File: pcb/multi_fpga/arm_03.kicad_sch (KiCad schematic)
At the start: 16 parts, among them U25 IM72D128V01XTMA1, U26 IM72D128V01XTMA1, U27 IM72D128V01XTMA1, U28 IM72D128V01XTMA1, U29 IM72D128V01XTMA1, U30 IM72D128V01XTMA1, U31 IM72D128V01XTMA1, U32 IM72D128V01XTMA1

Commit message: Fixed library and power issues.
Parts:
- C25, C26, C27, C28, C29, C30, C31, C32: symbol C -> multi_fpga:C
- U25, U26, U27, U28, U29, U30, U31, U32: symbol IM72D128 -> multi_fpga:IM72D128

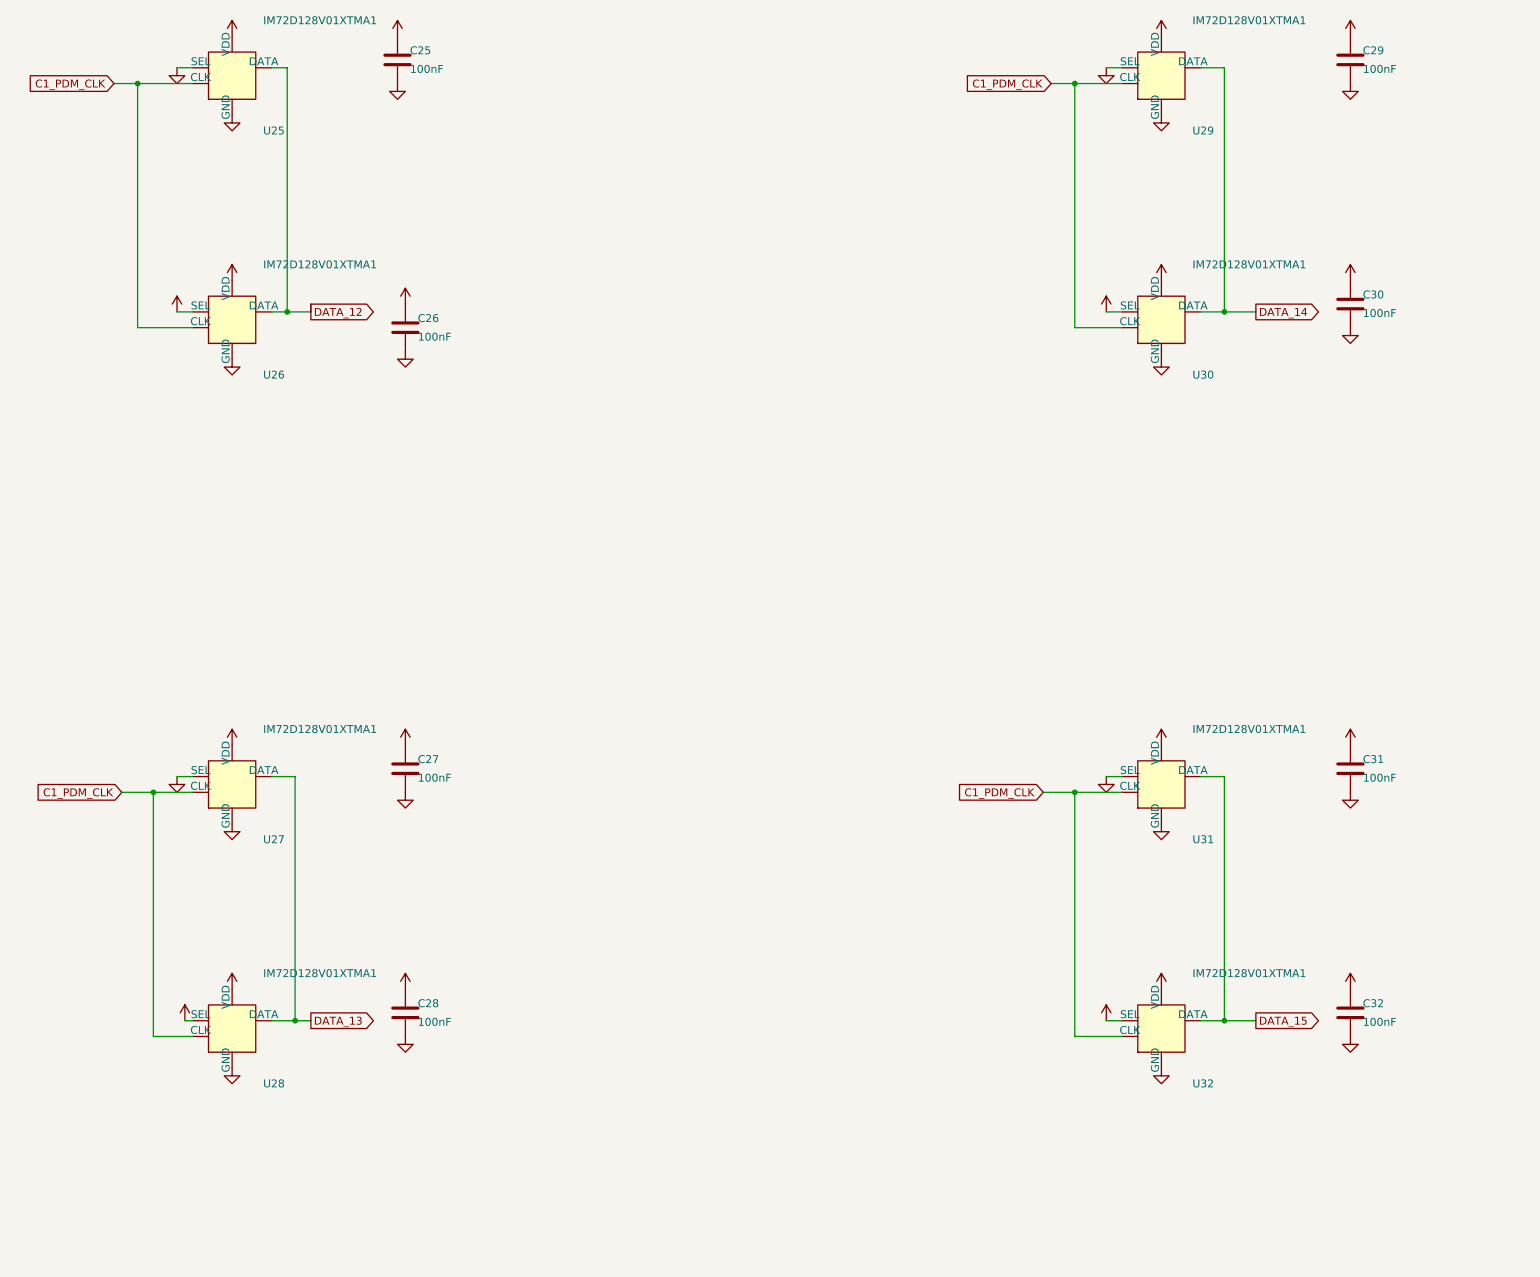
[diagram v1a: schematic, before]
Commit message: Fixed power and C ref des collisions.
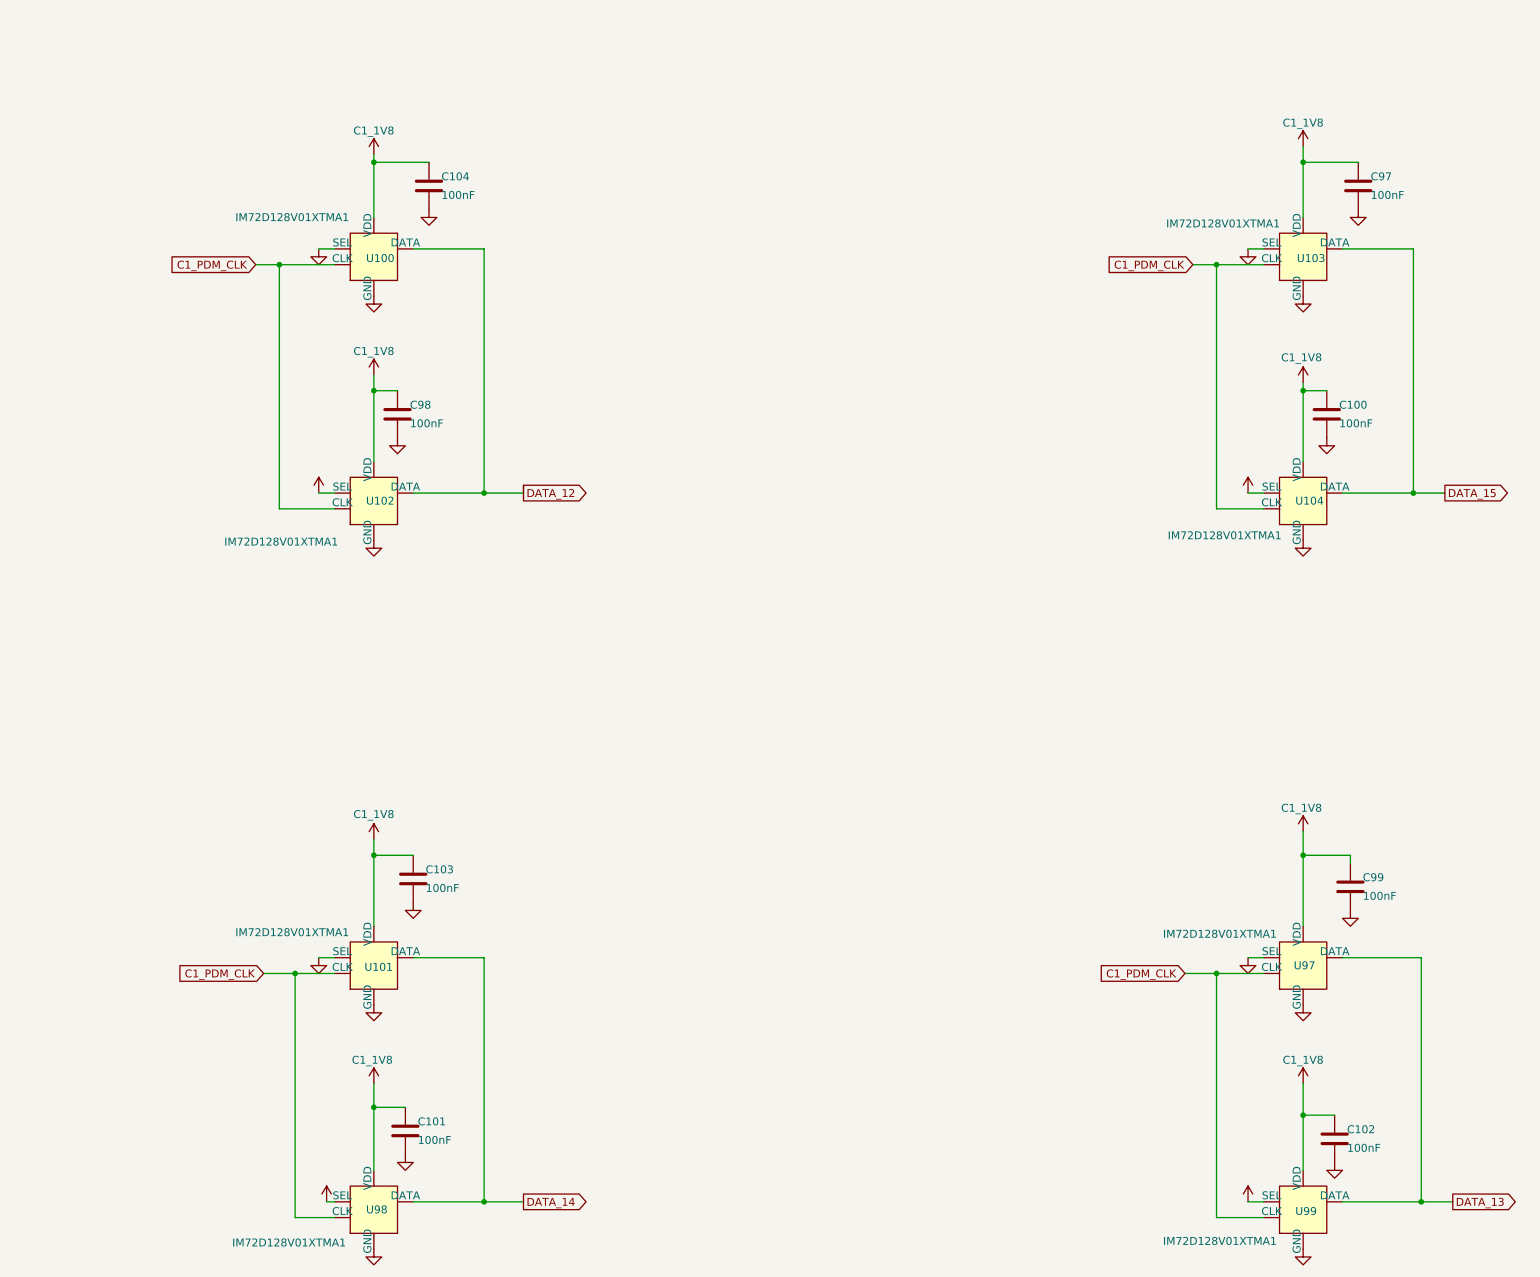
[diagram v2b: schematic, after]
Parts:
- removed C25, C26, C27, C28, C29, C30, C31, C32: 100nF, symbol multi_fpga:C
- removed U25, U26, U27, U28, U29, U30, U31, U32: IM72D128V01XTMA1, symbol multi_fpga:IM72D128
- added C100, C101, C102, C103, C104, C97, C98, C99: 100nF, symbol multi_fpga:C
- added U100, U101, U102, U103, U104, U97, U98, U99: IM72D128V01XTMA1, symbol multi_fpga:IM72D128
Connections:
- net C1_1V8: now also C100.1, C101.1, C102.1, C103.1, C104.1, C97.1, C98.1, C99.1, U100.2 (VDD), U101.2 (VDD), U102.2 (VDD), U102.4 (SEL), U103.2 (VDD), U104.2 (VDD), U104.4 (SEL), U97.2 (VDD), U98.2 (VDD), U98.4 (SEL), U99.2 (VDD), U99.4 (SEL)
- net C1_PDM_CLK: now also U100.3 (CLK), U101.3 (CLK), U102.3 (CLK), U103.3 (CLK), U104.3 (CLK), U97.3 (CLK), U98.3 (CLK), U99.3 (CLK)
- net DATA_12: now also U100.1 (DATA), U102.1 (DATA)
- net DATA_13: now also U97.1 (DATA), U99.1 (DATA)
- net DATA_14: now also U101.1 (DATA), U98.1 (DATA)
- net DATA_15: now also U103.1 (DATA), U104.1 (DATA)
- net GND: now also C100.2, C101.2, C102.2, C103.2, C104.2, C97.2, C98.2, C99.2, U100.4 (SEL), U100.5 (GND), U101.4 (SEL), U101.5 (GND), U102.5 (GND), U103.4 (SEL), U103.5 (GND), U104.5 (GND), U97.4 (SEL), U97.5 (GND), U98.5 (GND), U99.5 (GND)

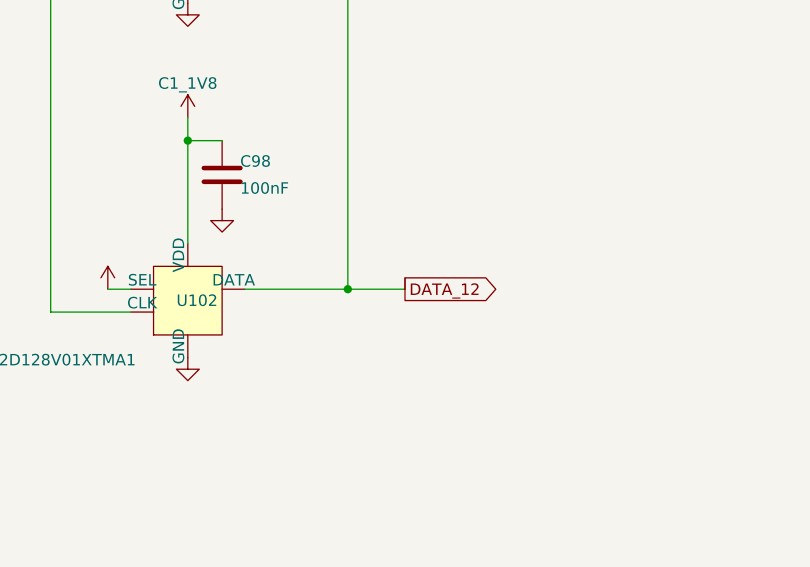
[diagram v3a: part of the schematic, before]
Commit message: Fixed regulator connection errors and dangling wire.
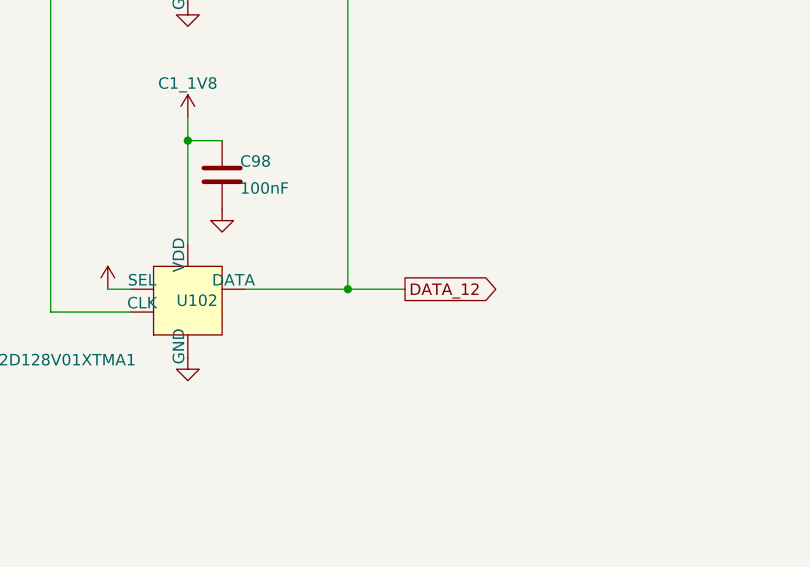
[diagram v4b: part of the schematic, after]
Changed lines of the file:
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@@
-	(wire
-		(pts
-			(xy 127 106.68) (xy 127 107.95)
-		)
-		(stroke
-			(width 0)
-			(type default)
-		)
-	)
 	(wire
 		(pts

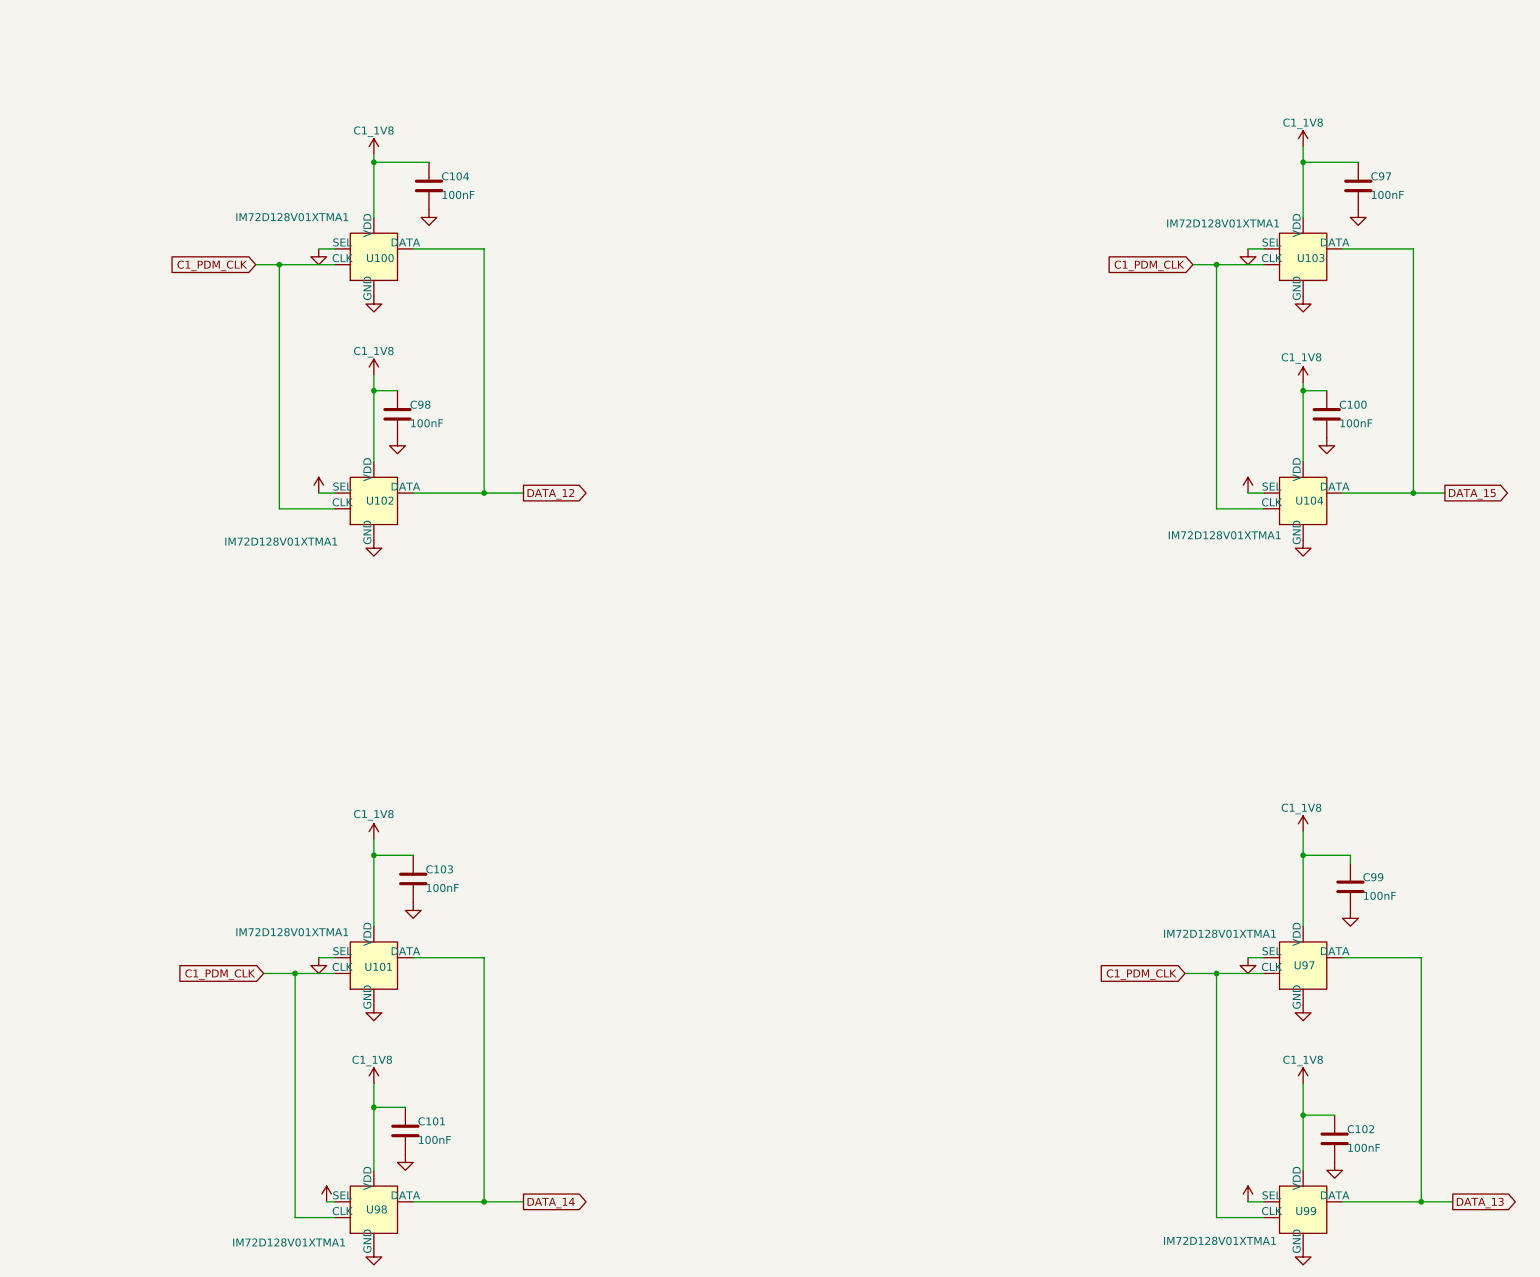
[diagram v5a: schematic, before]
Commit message: Global fix of res defs.
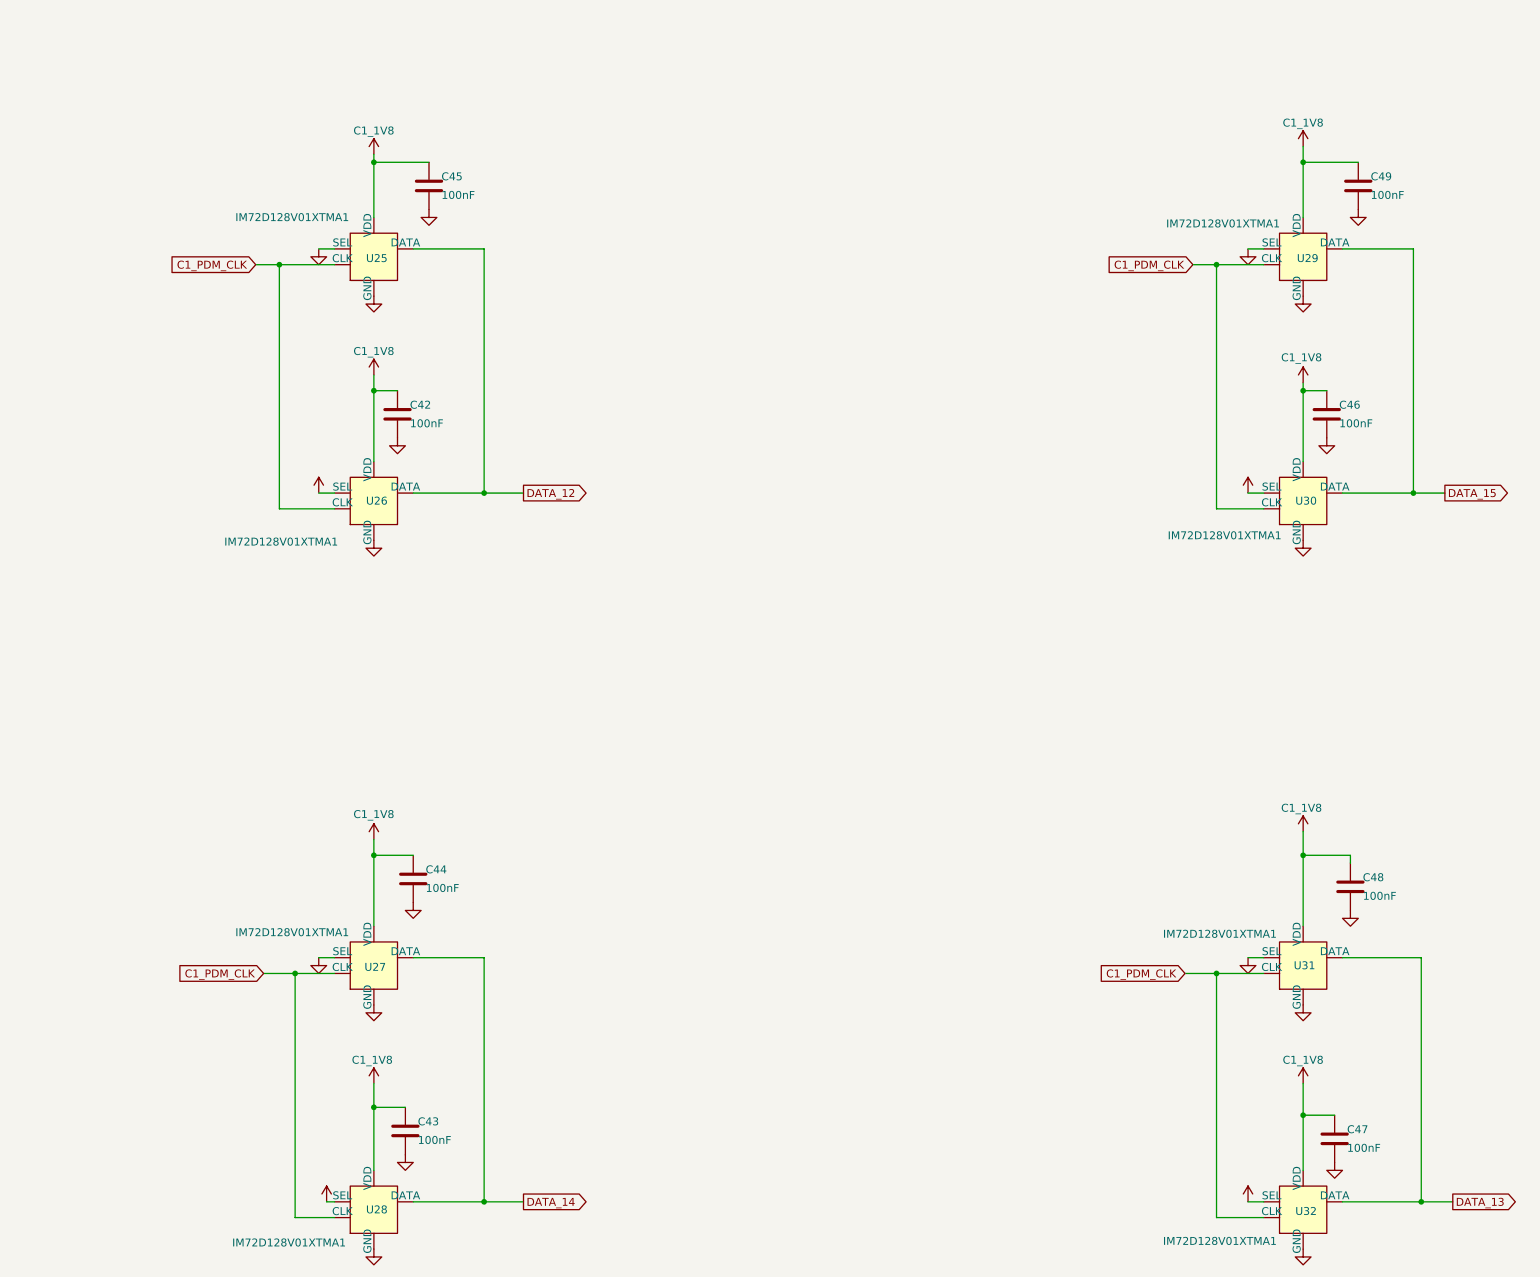
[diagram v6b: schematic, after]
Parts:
- renumbered C98 to C42, C101 to C43, C103 to C44, C104 to C45, C100 to C46, C102 to C47, C99 to C48, C97 to C49, U100 to U25, U102 to U26, U101 to U27, U98 to U28, U103 to U29, U104 to U30, U97 to U31, U99 to U32
